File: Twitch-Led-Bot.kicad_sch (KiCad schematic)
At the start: 29 parts, among them J1 USB4105-GF-A, Q1 BC847, Q2 BC847, SW1 Reset, U1 AMS1117-3.3, U2 CH340G, U3 ESP-12F, Y1 12MHz, Y2 CSTCE12M0G55-R0

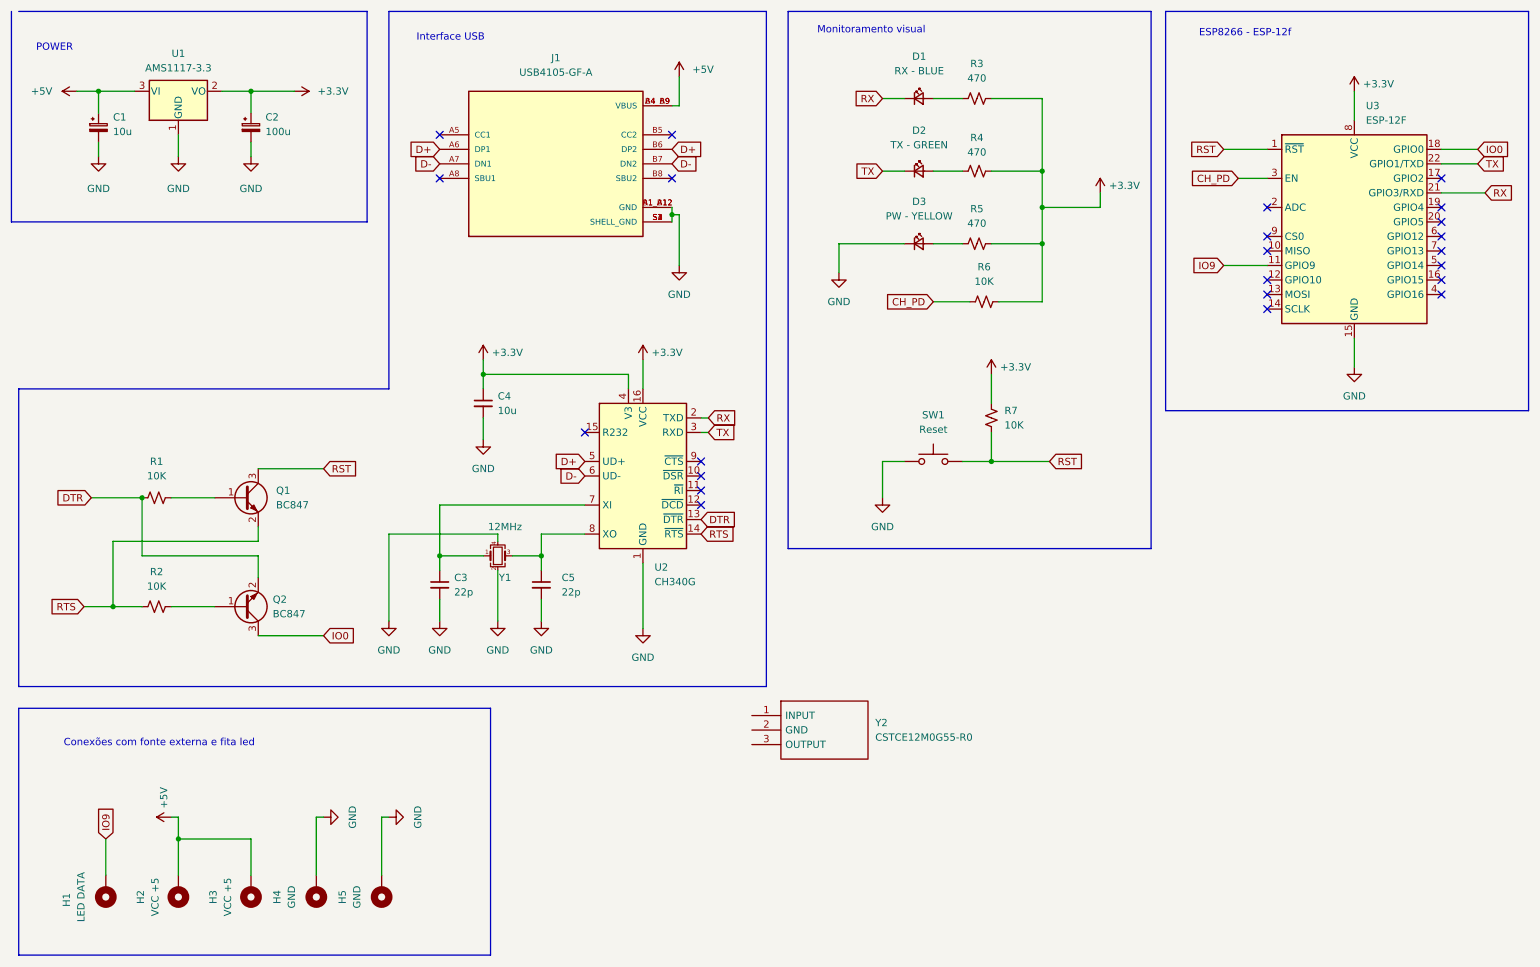
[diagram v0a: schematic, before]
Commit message: Bug correction v.1.0.1
Correction in the wiring diagram with the microcontroller connecting GP015 to GND
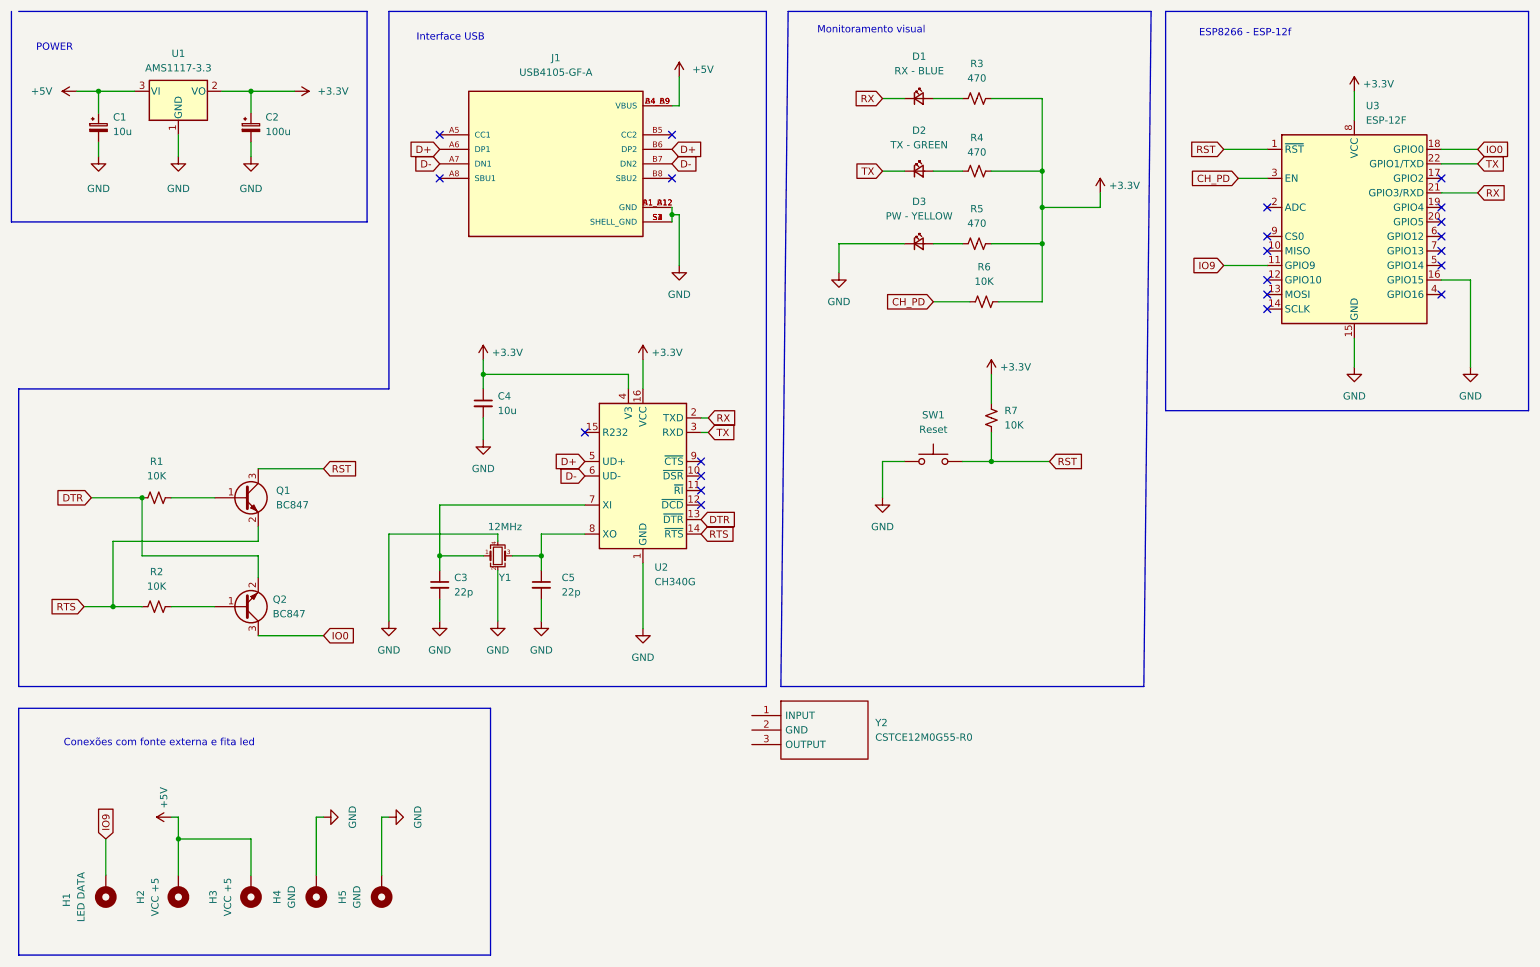
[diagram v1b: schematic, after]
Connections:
- net GND: now also U3.16 (GPIO15)
- no-connect marks 23 -> 22
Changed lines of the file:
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@@
   (no_connect (at 135.89 97.79))
   (no_connect (at 265.43 55.88))
-  (no_connect (at 265.43 63.5))
   (wire (pts (xy 52.07 30.48) (xy 57.15 30.48))
     (stroke (width 0) (type default) (color 0 0 0 0))
@@
     (stroke (width 0) (type default) (color 0 0 0 0))
   )
+  (wire (pts (xy 265.43 63.5) (xy 270.51 63.5))
+    (stroke (width 0) (type default) (color 0 0 0 0))
+  )
   (wire (pts (xy 186.69 95.25) (xy 196.85 95.25))
     (stroke (width 0) (type default) (color 0 0 0 0))
@@
     (stroke (width 0) (type default) (color 0 0 0 0))
   )
-  (polyline (pts (xy 151.13 16.51) (xy 151.13 110.49))
+  (polyline (pts (xy 151.13 16.51) (xy 149.86 134.62))
     (stroke (width 0) (type default) (color 0 0 0 0))
   )
@@
     (stroke (width 0) (type default) (color 0 0 0 0))
   )
-  (polyline (pts (xy 214.63 16.51) (xy 214.63 110.49))
+  (polyline (pts (xy 214.63 16.51) (xy 213.36 134.62))
     (stroke (width 0) (type default) (color 0 0 0 0))
   )
@@
     (stroke (width 0) (type default) (color 0 0 0 0))
   )
+  (wire (pts (xy 270.51 63.5) (xy 270.51 78.74))
+    (stroke (width 0) (type default) (color 0 0 0 0))
+  )
   (wire (pts (xy 195.58 44.45) (xy 195.58 50.8))
     (stroke (width 0) (type default) (color 0 0 0 0))
@@
     (stroke (width 0) (type default) (color 0 0 0 0))
   )
-  (wire (pts (xy 265.43 48.26) (xy 273.05 48.26))
+  (wire (pts (xy 265.43 48.26) (xy 271.78 48.26))
     (stroke (width 0) (type default) (color 0 0 0 0))
   )
@@
     (stroke (width 0) (type default) (color 0 0 0 0))
   )
-  (polyline (pts (xy 214.63 110.49) (xy 151.13 110.49))
+  (polyline (pts (xy 213.36 134.62) (xy 149.86 134.62))
     (stroke (width 0) (type default) (color 0 0 0 0))
   )
@@
     )
   )
-  (global_label "RX" (shape input) (at 273.05 48.26 0) (fields_autoplaced)
+  (global_label "RX" (shape input) (at 271.78 48.26 0) (fields_autoplaced)
     (effects (font (size 1.27 1.27)) (justify left))
-    (property "Referências entre as folhas" "${INTERSHEET_REFS}" (id 0) (at 277.9426 48.1806 0)
+    (property "Referências entre as folhas" "${INTERSHEET_REFS}" (id 0) (at 276.6726 48.1806 0)
       (effects (font (size 1.27 1.27)) (justify left) hide)
     )
@@
     (pin "8")
     (pin "9")
+  )
+  (symbol (lib_name "GND_1") (lib_id "power:GND") (at 270.51 78.74 0) (unit 1)
+    (in_bom yes) (on_board yes) (fields_autoplaced)
+    (property "Reference" "#PWR0101" (id 0) (at 270.51 85.09 0)
+      (effects (font (size 1.27 1.27)) hide)
+    )
+    (property "Value" "GND" (id 1) (at 270.51 83.82 0))
+    (property "Footprint" "" (id 2) (at 270.51 78.74 0)
+      (effects (font (size 1.27 1.27)) hide)
+    )
+    (property "Datasheet" "" (id 3) (at 270.51 78.74 0)
+      (effects (font (size 1.27 1.27)) hide)
+    )
+    (pin "1")
   )
   (symbol (lib_id "power:GND") (at 44.45 41.91 0) (unit 1)
@@
       (reference "#PWR024") (unit 1) (value "GND") (footprint "")
     )
+    (path "/052a2e6a-ba60-4359-856f-34717d9df3bb"
+      (reference "#PWR0101") (unit 1) (value "GND") (footprint "")
+    )
     (path "/577abdac-800b-4fde-9625-5878b3277845"
